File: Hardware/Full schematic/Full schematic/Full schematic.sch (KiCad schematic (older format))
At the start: 326 parts, among them J1 Conn_01x02_Male, J2 Reset, J3 Encoder, J4 Failure LED, J5 Bluetooth, J6 Conn_01x02_Male, J7 Display, J8 Buttons, J9 Conn_01x02_Male, K1 EDR101A0500, K2 EDR101A0500, K3 EDR101A0500, K4 EDR101A0500, K5 EDR101A0500, K6 EDR101A0500, Q1 BC847, Q10 IRLML6402, Q11 BC847, Q12 IRFZ44, Q13 BC847, Q14 BSS138, Q15 BC847, Q16 IRF610, Q17 BC847, Q18 IRLML6402, Q19 BC847, Q2 BC847, Q20 BFS17, Q21 IRLML6402, Q22 AFT05MS003N, Q23 IRLML2502, Q24 IRLML2502, Q25 IRLML2502, Q26 IRLML2502, Q27 IRLML2502, Q28 IRLML2502, Q3 BC847, Q4 BC847, Q5 BC847, Q6 IRLML6402, Q7 IRF4905, Q8 IRLML6402, Q9 IRLML6402, U1 74LVC2T45DC, U10 ICS501, U11 STM32F103C8Tx, U12 CAT24C256, U2 74LVC2T45DC, U3 AD9835, U4 LM27313XMF, U5 LM2734X, U6 LM2734X, U7 LM2734X, U8 UC3843_SOIC8, U9 AD5245BRJZ10, X1 50MHz, Y1 8MHz, Y2 32768Hz

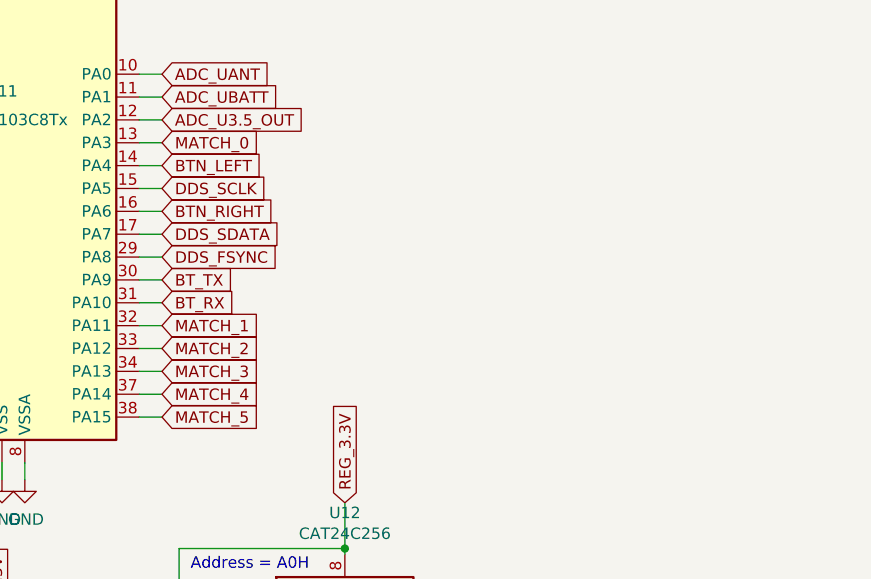
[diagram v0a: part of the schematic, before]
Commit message: Added programming connector
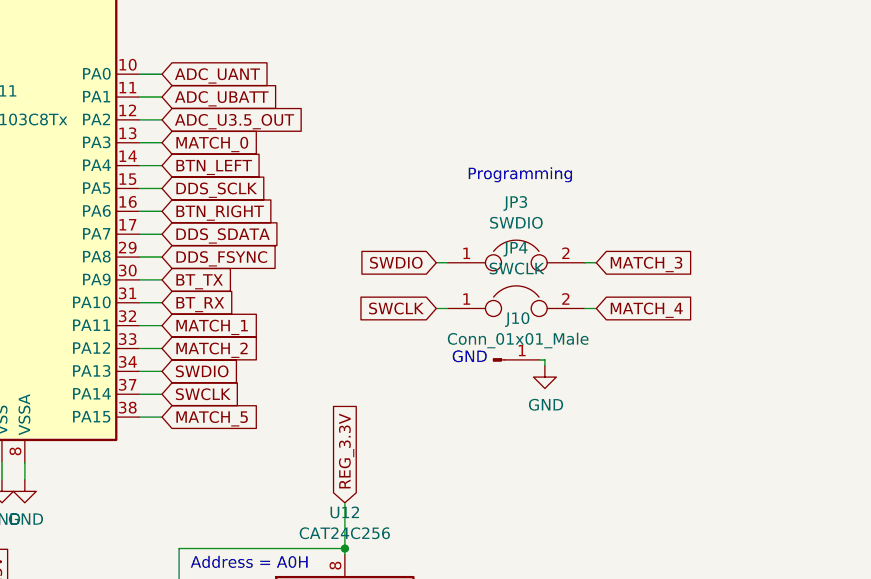
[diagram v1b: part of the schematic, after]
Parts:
- added J10: Conn_01x01_Male, symbol Connector:Conn_01x01_Male
- added JP3: SWDIO, symbol Device:Jumper
- added JP4: SWCLK, symbol Device:Jumper
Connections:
- net GND: now also J10.1 (Pin_1)
- net MATCH_3: now also JP3.2; no longer U11.34 (PA13)
- net MATCH_4: now also JP4.2; no longer U11.37 (PA14)
- new net SWCLK: JP4.1, U11.37 (PA14)
- new net SWDIO: JP3.1, U11.34 (PA13)
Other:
- note added: "Programming"
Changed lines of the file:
@@
 $EndComp
 $Comp
-L power:GND #PWR0168
+L power:GND #PWR0169
 U 1 1 5FF8781C
 P 19750 4075
-F 0 "#PWR0168" H 19750 3825 50  0001 C CNN
+F 0 "#PWR0169" H 19750 3825 50  0001 C CNN
 F 1 "GND" H 19755 3902 50  0000 C CNN
 F 2 "" H 19750 4075 50  0001 C CNN
@@
 $EndComp
 $Comp
-L power:GND #PWR0170
+L power:GND #PWR0171
 U 1 1 5FF9177C
 P 20750 4075
-F 0 "#PWR0170" H 20750 3825 50  0001 C CNN
+F 0 "#PWR0171" H 20750 3825 50  0001 C CNN
 F 1 "GND" H 20755 3902 50  0000 C CNN
 F 2 "" H 20750 4075 50  0001 C CNN
@@
 $EndComp
 $Comp
-L power:GND #PWR0169
+L power:GND #PWR0170
 U 1 1 6008B90A
 P 20150 4775
-F 0 "#PWR0169" H 20150 4525 50  0001 C CNN
+F 0 "#PWR0170" H 20150 4525 50  0001 C CNN
 F 1 "GND" H 20155 4602 50  0000 C CNN
 F 2 "" H 20150 4775 50  0001 C CNN
@@
 $EndComp
 $Comp
-L power:GND #PWR0171
+L power:GND #PWR0172
 U 1 1 600A46A1
 P 21150 4775
-F 0 "#PWR0171" H 21150 4525 50  0001 C CNN
+F 0 "#PWR0172" H 21150 4525 50  0001 C CNN
 F 1 "GND" H 21155 4602 50  0000 C CNN
 F 2 "" H 21150 4775 50  0001 C CNN
@@
 $EndComp
 $Comp
-L power:GND #PWR0172
+L power:GND #PWR0173
 U 1 1 6017CE01
 P 21750 4075
-F 0 "#PWR0172" H 21750 3825 50  0001 C CNN
+F 0 "#PWR0173" H 21750 3825 50  0001 C CNN
 F 1 "GND" H 21755 3902 50  0000 C CNN
 F 2 "" H 21750 4075 50  0001 C CNN
@@
 $EndComp
 $Comp
-L power:GND #PWR0173
+L power:GND #PWR0174
 U 1 1 6017CE10
 P 22150 4775
-F 0 "#PWR0173" H 22150 4525 50  0001 C CNN
+F 0 "#PWR0174" H 22150 4525 50  0001 C CNN
 F 1 "GND" H 22155 4602 50  0000 C CNN
 F 2 "" H 22150 4775 50  0001 C CNN
@@
 Text GLabel 17750 14850 2    50   Input ~ 0
 MATCH_2
-Text GLabel 17750 14950 2    50   Input ~ 0
+Text GLabel 19650 14475 2    50   Input ~ 0
 MATCH_3
-Text GLabel 17750 15050 2    50   Input ~ 0
+Text GLabel 19650 14675 2    50   Input ~ 0
 MATCH_4
 Text GLabel 17750 15150 2    50   Input ~ 0
@@
 	1    0    0    -1
 $EndComp
+Text GLabel 17750 14950 2    50   Input ~ 0
+SWDIO
+Text GLabel 17750 15050 2    50   Input ~ 0
+SWCLK
+$Comp
+L Device:Jumper JP3
+U 1 1 60DF3F8E
+P 19300 14475
+F 0 "JP3" H 19300 14739 50  0000 C CNN
+F 1 "SWDIO" H 19300 14648 50  0000 C CNN
+F 2 "" H 19300 14475 50  0001 C CNN
+F 3 "~" H 19300 14475 50  0001 C CNN
+	1    19300 14475
+	1    0    0    -1
+$EndComp
+$Comp
+L Device:Jumper JP4
+U 1 1 60DF5542
+P 19300 14675
+F 0 "JP4" H 19300 14939 50  0000 C CNN
+F 1 "SWCLK" H 19300 14848 50  0000 C CNN
+F 2 "" H 19300 14675 50  0001 C CNN
+F 3 "~" H 19300 14675 50  0001 C CNN
+	1    19300 14675
+	1    0    0    -1
+$EndComp
+Wire Wire Line
+	19650 14475 19600 14475
+Wire Wire Line
+	19650 14675 19600 14675
+Text GLabel 18950 14475 0    50   Input ~ 0
+SWDIO
+Text GLabel 18950 14675 0    50   Input ~ 0
+SWCLK
+Wire Wire Line
+	18950 14475 19000 14475
+Wire Wire Line
+	19000 14675 18950 14675
+$Comp
+L Connector:Conn_01x01_Male J10
+U 1 1 613EB795
+P 19200 14900
+F 0 "J10" H 19308 15081 50  0000 C CNN
+F 1 "Conn_01x01_Male" H 19308 14990 50  0000 C CNN
+F 2 "" H 19200 14900 50  0001 C CNN
+F 3 "~" H 19200 14900 50  0001 C CNN
+	1    19200 14900
+	1    0    0    -1
+$EndComp
+$Comp
+L power:GND #PWR0168
+U 1 1 613EC935
+P 19425 14925
+F 0 "#PWR0168" H 19425 14675 50  0001 C CNN
+F 1 "GND" H 19430 14752 50  0000 C CNN
+F 2 "" H 19425 14925 50  0001 C CNN
+F 3 "" H 19425 14925 50  0001 C CNN
+	1    19425 14925
+	1    0    0    -1
+$EndComp
+Wire Wire Line
+	19425 14925 19425 14900
+Wire Wire Line
+	19425 14900 19400 14900
+Text Notes 19175 14925 2    50   ~ 0
+GND
+Text Notes 19550 14125 2    50   ~ 0
+Programming
 $EndSCHEMATC

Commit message: Assigned cases to parts, ready to trace PCB
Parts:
- C1, C48, C49, C50: footprint (none) -> Capacitor_THT:CP_Radial_D6.3mm_P2.50mm
- C10, C11, C12, C9: footprint (none) -> Capacitor_THT:CP_Radial_D4.0mm_P2.00mm
- C100, C108, C109, C13, C14, C15, C16, C19, C20, C23, C25, C26, C27, C28, C30, C32, C33, C34, C35, C37, C38, C39, C41, C42, C43, C45, C46, C47, C51, C52, C55, C57, C6, C60, C64, C67, C70, C76, C78, C79, C80, C81, C82, C83, C85, C86, C93, C94, C95, C98: footprint (none) -> Capacitor_SMD:C_0805_2012Metric_Pad1.18x1.45mm_HandSolder
- C110: footprint Capacitor_THT:CP_Radial_D8.0mm_P3.80mm -> Capacitor_THT:CP_Radial_D6.3mm_P2.50mm
- C111: footprint Capacitor_THT:CP_Radial_D8.0mm_P3.80mm -> Capacitor_THT:CP_Radial_D4.0mm_P2.00mm
- C17: value 2.2uF -> 4.7uF; footprint (none) -> Capacitor_SMD:C_0805_2012Metric_Pad1.18x1.45mm_HandSolder
- C29, C53, C58: footprint (none) -> Capacitor_THT:CP_Radial_D10.0mm_P5.00mm
- C40: footprint (none) -> Capacitor_Tantalum_SMD:CP_EIA-7132-28_AVX-C_Pad2.72x3.50mm_HandSolder
- C75: value 470uFx6.3V -> 100uFx6.3V; footprint Capacitor_THT:CP_Radial_D8.0mm_P3.80mm -> Capacitor_THT:CP_Radial_D6.3mm_P2.50mm
- D11: value 1N4148 -> 1N4148W; footprint (none) -> Diode_SMD:D_SOD-123
- D12: footprint (none) -> Diode_THT:D_DO-27_P5.08mm_Vertical_AnodeUp
- D4, D5, D6, D7: footprint (none) -> Diode_SMD:D_SOD-123
- J1, J2, J4, JP3, JP4: footprint (none) -> Connector_PinHeader_2.54mm:PinHeader_1x02_P2.54mm_Vertical
- J10: footprint (none) -> Connector_PinHeader_2.54mm:PinHeader_1x01_P2.54mm_Vertical
- J3, J5, J7: footprint (none) -> Connector_PinHeader_2.54mm:PinHeader_1x04_P2.54mm_Vertical
- J8, JP1, JP2: footprint (none) -> Connector_PinHeader_2.54mm:PinHeader_1x03_P2.54mm_Vertical
- L1, L3, L4, L5: footprint (none) -> Inductor_SMD:L_1812_4532Metric_Pad1.30x3.40mm_HandSolder
- L10: footprint (none) -> Inductor_SMD:L_12x12mm_H8mm
- L2, L6, L7, L9: footprint Inductor_THT:L_Radial_D9.5mm_P5.00mm_Fastron_07HVP -> Inductor_SMD:L_1812_4532Metric_Pad1.30x3.40mm_HandSolder
- L8: footprint (none) -> Inductor_THT:L_Toroid_Vertical_L25.4mm_W14.7mm_P12.20mm_Vishay_TJ5_BigPads
- Q12: footprint (none) -> Package_TO_SOT_THT:TO-220-3_Vertical
- R10, R11, R12, R13, R14, R15, R16, R17, R18, R19, R20, R21, R22, R23, R24, R28, R29, R30, R32, R34, R35, R36, R37, R38, R39, R4, R40, R41, R42, R43, R44, R5, R55, R56, R6, R66, R67, R68, R69, R7, R73, R74, R78, R79, R8, R80, R81, R84, R85, R86, R87, R88, R9, R90, R91, R92: footprint (none) -> Resistor_SMD:R_0805_2012Metric_Pad1.20x1.40mm_HandSolder
- R45, R46, R47, R49: footprint (none) -> Resistor_THT:R_Axial_DIN0207_L6.3mm_D2.5mm_P2.54mm_Vertical
- U1, U2: footprint Package_SO:SSOP-8_2.95x2.8mm_P0.65mm -> Package_SO:VSSOP-8_2.3x2mm_P0.5mm
- U12: footprint (none) -> Package_SO:SOIC-8_5.23x5.23mm_P1.27mm
- U9: footprint (none) -> Package_TO_SOT_SMD:SOT-23-8_Handsoldering
- Y1: footprint (none) -> Crystal:Crystal_HC49-U_Vertical
- Y2: footprint (none) -> Crystal:Crystal_C26-LF_D2.1mm_L6.5mm_Horizontal_1EP_style1
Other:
- note added: "1 - Off\n0 - On"
- note added: "1 - On\n0 - Off"

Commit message: PCB tracing in progress
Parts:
- L11: footprint Inductor_THT:L_Radial_D9.5mm_P5.00mm_Fastron_07HVP -> Inductor_SMD:L_1812_4532Metric_Pad1.30x3.40mm_HandSolder
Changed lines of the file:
@@
 F 0 "L11" H 12903 1946 50  0000 L CNN
 F 1 "10uH" H 12903 1855 50  0000 L CNN
-F 2 "Inductor_THT:L_Radial_D9.5mm_P5.00mm_Fastron_07HVP" H 12850 1900 50  0001 C CNN
+F 2 "Inductor_SMD:L_1812_4532Metric_Pad1.30x3.40mm_HandSolder" H 12850 1900 50  0001 C CNN
 F 3 "~" H 12850 1900 50  0001 C CNN
 	1    12850 1900

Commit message: U80m calibration
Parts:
- R56: value 4.3k -> 4.7k
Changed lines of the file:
@@
 P 11075 11975
 F 0 "R56" H 11145 12021 50  0000 L CNN
-F 1 "4.3k" H 11145 11930 50  0000 L CNN
+F 1 "4.7k" H 11145 11930 50  0000 L CNN
 F 2 "Resistor_SMD:R_0805_2012Metric_Pad1.20x1.40mm_HandSolder" V 11005 11975 50  0001 C CNN
 F 3 "~" H 11075 11975 50  0001 C CNN

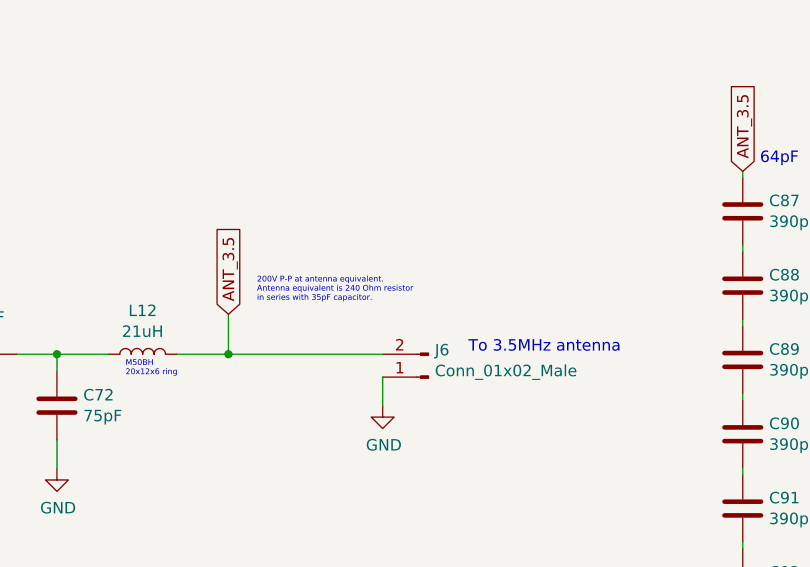
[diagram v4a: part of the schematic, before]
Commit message: Added information on antenna equivalents
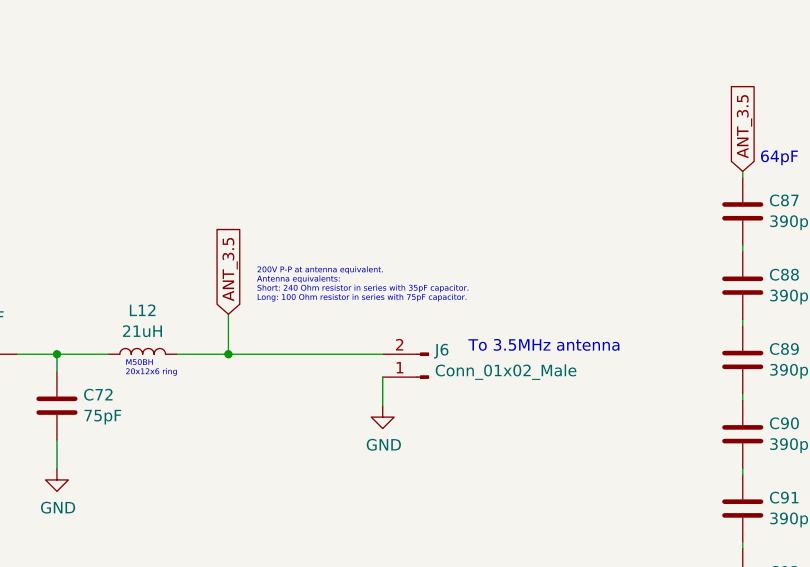
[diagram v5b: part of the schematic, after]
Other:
- note added: "200V P-P at antenna equivalent.\nAntenna equivalents:\nShort: 240 Ohm resistor in series with 35pF capacitor. \nLong: 100 Ohm resistor in series with 75pF capacitor."
- note removed: "200V P-P at antenna equivalent.\nAntenna equivalent is 240 Ohm resistor\nin series with 35pF capacitor."
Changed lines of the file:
@@
 	14500 1975 14500 2150
 Text Notes 14625 1925 0    25   ~ 0
-200V P-P at antenna equivalent.\nAntenna equivalent is 240 Ohm resistor\nin series with 35pF capacitor.
+200V P-P at antenna equivalent.\nAntenna equivalents:\nShort: 240 Ohm resistor in series with 35pF capacitor. \nLong: 100 Ohm resistor in series with 75pF capacitor.
 Text GLabel 13400 3300 1    50   Input ~ 0
 ANT_3.5

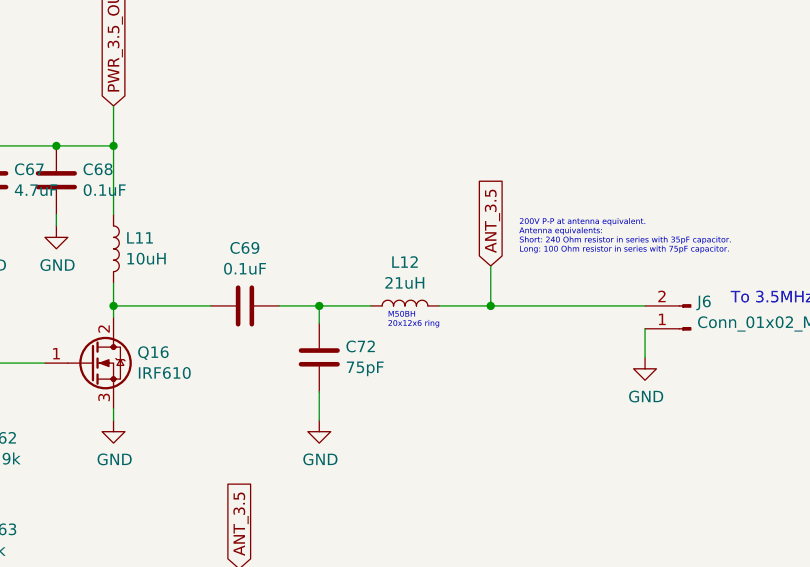
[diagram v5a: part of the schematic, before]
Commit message: Updated L12 value for matching with antennas of different lengths
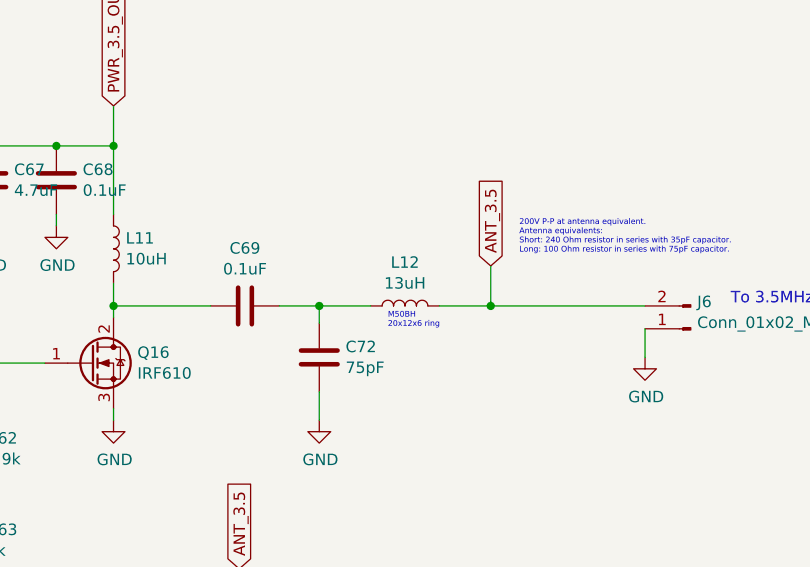
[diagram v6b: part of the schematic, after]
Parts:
- L12: value 21uH -> 13uH
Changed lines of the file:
@@
 P 14125 2150
 F 0 "L12" V 14315 2150 50  0000 C CNN
-F 1 "21uH" V 14224 2150 50  0000 C CNN
+F 1 "13uH" V 14224 2150 50  0000 C CNN
 F 2 "Inductor_THT:L_Toroid_Vertical_L21.6mm_W9.1mm_P8.40mm_Bourns_5700" H 14125 2150 50  0001 C CNN
 F 3 "~" H 14125 2150 50  0001 C CNN

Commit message: After system reinstallation (different version of KiCAD)
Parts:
- DA1: symbol Fossa_library:AD825 -> Full-schematic-rescue:AD825-Fossa_library
- K1, K2, K3, K4, K5, K6: symbol Fossa_library:EDR101A0500 -> Full-schematic-rescue:EDR101A0500-Fossa_library
- U10: symbol Fossa_library:ICS501 -> Full-schematic-rescue:ICS501-Fossa_library
- U3: symbol Fossa_library:AD9835 -> Full-schematic-rescue:AD9835-Fossa_library
- U9: symbol Fossa_library:AD5245 -> Full-schematic-rescue:AD5245-Fossa_library
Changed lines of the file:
@@
 $EndDescr
 $Comp
-L Fossa_library:AD9835 U3
+L Full-schematic-rescue:AD9835-Fossa_library U3
 U 1 1 5FDCFB3A
 P 5675 2525
@@
 Connection ~ 8675 3725
 $Comp
-L Fossa_library:AD825 DA1
+L Full-schematic-rescue:AD825-Fossa_library DA1
 U 1 1 5FE6E843
 P 11825 2400
@@
 	15175 2375 15175 2250
 $Comp
-L Fossa_library:EDR101A0500 K1
+L Full-schematic-rescue:EDR101A0500-Fossa_library K1
 U 1 1 5FF371A8
 P 16950 3700
@@
 	16750 4075 16750 4000
 $Comp
-L Fossa_library:EDR101A0500 K2
+L Full-schematic-rescue:EDR101A0500-Fossa_library K2
 U 1 1 5FF59BA9
 P 17950 3700
@@
 	17750 4075 17750 4000
 $Comp
-L Fossa_library:EDR101A0500 K3
+L Full-schematic-rescue:EDR101A0500-Fossa_library K3
 U 1 1 5FF7E77F
 P 18950 3700
@@
 	18750 4075 18750 4000
 $Comp
-L Fossa_library:EDR101A0500 K4
+L Full-schematic-rescue:EDR101A0500-Fossa_library K4
 U 1 1 5FF87815
 P 19950 3700
@@
 	19750 4075 19750 4000
 $Comp
-L Fossa_library:EDR101A0500 K5
+L Full-schematic-rescue:EDR101A0500-Fossa_library K5
 U 1 1 5FF91775
 P 20950 3700
@@
 	11250 3675 11250 2650
 $Comp
-L Fossa_library:EDR101A0500 K6
+L Full-schematic-rescue:EDR101A0500-Fossa_library K6
 U 1 1 6017CDFB
 P 21950 3700
@@
 $EndComp
 $Comp
-L Fossa_library:ICS501 U10
+L Full-schematic-rescue:ICS501-Fossa_library U10
 U 1 1 60193519
 P 13825 7075
@@
 $EndComp
 $Comp
-L Fossa_library:AD5245 U9
+L Full-schematic-rescue:AD5245-Fossa_library U9
 U 1 1 610BB3C9
 P 11525 12150
